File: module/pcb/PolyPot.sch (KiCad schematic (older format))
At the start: 43 parts, among them J1 V_BAT_1S, J2 PROG/DEBUG, J3 HUMIDITY_CONN, J4 TOF_DIST_SENS, J5 M3, J6 M3, J7 M3, J8 M3, J9 LUMINOSITY_CONN, M1 DC_WATER_PUMP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

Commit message: PCB: change SOIC-8 footprint
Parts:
- U4: footprint Housings_SOIC:SO-8_5.3x6.2mm_Pitch1.27mm -> Housings_SOIC:SOIC-8_3.9x4.9mm_Pitch1.27mm
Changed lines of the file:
@@
 F 0 "U4" H 4950 1650 60  0000 C CNN
 F 1 "BD6211F-E2" H 5650 1650 60  0000 C CNN
-F 2 "Housings_SOIC:SO-8_5.3x6.2mm_Pitch1.27mm" H 5300 1400 60  0001 C CNN
+F 2 "Housings_SOIC:SOIC-8_3.9x4.9mm_Pitch1.27mm" H 5300 1400 60  0001 C CNN
 F 3 "" H 5300 1400 60  0001 C CNN
 	1    5300 1400

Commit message: Add logo
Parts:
- removed TP1, TP2, TP3, TP4, TP5: TEST, Socket_Strips:Socket_Strip_Straight_1x01_Pitch1.27mm, symbol TEST
- added J10: I2C_TEST, Pin_Headers:Pin_Header_Straight_1x02_Pitch2.54mm, symbol Conn_01x02
- BT1, M1: footprint Socket_Strips:Socket_Strip_Straight_1x02_Pitch2.54mm -> Pin_Headers:Pin_Header_Straight_1x02_Pitch2.54mm
- J1: footprint Socket_Strips:Socket_Strip_Straight_1x01_Pitch2.54mm -> Pin_Headers:Pin_Header_Straight_1x01
- J2: footprint Socket_Strips:Socket_Strip_Straight_1x06_Pitch2.00mm -> Pin_Headers:Pin_Header_Straight_1x06_Pitch2.00mm
- J3, J9: footprint Socket_Strips:Socket_Strip_Straight_1x03_Pitch2.00mm -> Pin_Headers:Pin_Header_Straight_1x03_Pitch2.54mm
- J4: footprint Socket_Strips:Socket_Strip_Straight_1x05_Pitch2.00mm -> Pin_Headers:Pin_Header_Straight_1x05_Pitch2.54mm
- JP1, JP2: footprint Socket_Strips:Socket_Strip_Straight_1x02_Pitch1.27mm -> Pin_Headers:Pin_Header_Straight_1x02_Pitch2.54mm
- Q2: footprint TO_SOT_Packages_SMD:SOT-23 -> TO_SOT_Packages_SMD:SOT-23_Handsoldering
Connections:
- net I2C_SCL: now also J10.1 (Pin_1)
- net I2C_SDA: now also J10.2 (Pin_2)
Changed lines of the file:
@@
 LIBS:valves
 LIBS:PolyPot
+LIBS:PolyPot-cache
 EELAYER 25 0
 EELAYER END
@@
 F 0 "BT1" H 1200 1450 50  0000 L CNN
 F 1 "Battery" H 1200 1350 50  0000 L CNN
-F 2 "Socket_Strips:Socket_Strip_Straight_1x02_Pitch2.54mm" V 1100 1410 50  0001 C CNN
+F 2 "Pin_Headers:Pin_Header_Straight_1x02_Pitch2.54mm" V 1100 1410 50  0001 C CNN
 F 3 "" V 1100 1410 50  0001 C CNN
 	1    1100 1350
@@
 F 0 "JP1" H 1550 1230 50  0000 C CNN
 F 1 "I_SENSE" H 1560 1090 50  0000 C CNN
-F 2 "Socket_Strips:Socket_Strip_Straight_1x02_Pitch1.27mm" H 1550 1150 50  0001 C CNN
+F 2 "Pin_Headers:Pin_Header_Straight_1x02_Pitch2.54mm" H 1550 1150 50  0001 C CNN
 F 3 "" H 1550 1150 50  0001 C CNN
 	1    1550 1150
@@
 	1    0    0    -1
 $EndComp
-Text Label 8250 3350 2    60   ~ 0
+Text Label 7050 3300 0    60   ~ 0
 I2C_SDA
-Text Label 8250 3200 2    60   ~ 0
+Text Label 7050 3200 0    60   ~ 0
 I2C_SCL
 $Comp
@@
 F 0 "Q2" H 7950 1450 50  0000 L CNN
 F 1 "PMV250EPEAR" H 7950 1350 50  0000 L CNN
-F 2 "TO_SOT_Packages_SMD:SOT-23" H 7950 1500 50  0001 C CNN
+F 2 "TO_SOT_Packages_SMD:SOT-23_Handsoldering" H 7950 1500 50  0001 C CNN
 F 3 "" H 7750 1400 50  0001 C CNN
 	1    7750 1400
@@
 $EndComp
 $Comp
-L TEST TP2
-U 1 1 59FFB685
-P 7250 3200
-F 0 "TP2" H 7250 3500 50  0000 C BNN
-F 1 "TEST" H 7250 3450 50  0000 C CNN
-F 2 "Socket_Strips:Socket_Strip_Straight_1x01_Pitch1.27mm" H 7250 3200 50  0001 C CNN
-F 3 "" H 7250 3200 50  0001 C CNN
-	1    7250 3200
-	1    0    0    -1
-$EndComp
-$Comp
-L TEST TP1
-U 1 1 59FFB782
-P 7050 3350
-F 0 "TP1" H 7050 3650 50  0000 C BNN
-F 1 "TEST" H 7050 3600 50  0000 C CNN
-F 2 "Socket_Strips:Socket_Strip_Straight_1x01_Pitch1.27mm" H 7050 3350 50  0001 C CNN
-F 3 "" H 7050 3350 50  0001 C CNN
-	1    7050 3350
-	1    0    0    -1
-$EndComp
-$Comp
 L Jumper_NC_Small JP2
 U 1 1 59FFBC93
@@
 F 0 "JP2" H 8200 1380 50  0000 C CNN
 F 1 "I_SENSE" H 8210 1240 50  0000 C CNN
-F 2 "Socket_Strips:Socket_Strip_Straight_1x02_Pitch1.27mm" H 8200 1300 50  0001 C CNN
+F 2 "Pin_Headers:Pin_Header_Straight_1x02_Pitch2.54mm" H 8200 1300 50  0001 C CNN
 F 3 "" H 8200 1300 50  0001 C CNN
 	1    8200 1300
@@
 F 0 "J4" H 10300 3350 50  0000 C CNN
 F 1 "TOF_DIST_SENS" H 10300 2750 50  0000 C CNN
-F 2 "Socket_Strips:Socket_Strip_Straight_1x05_Pitch2.00mm" H 10300 3050 50  0001 C CNN
+F 2 "Pin_Headers:Pin_Header_Straight_1x05_Pitch2.54mm" H 10300 3050 50  0001 C CNN
 F 3 "" H 10300 3050 50  0001 C CNN
 	1    10300 3050
@@
 F 0 "M1" H 6200 1600 50  0000 L CNN
 F 1 "DC_WATER_PUMP" H 6200 1300 50  0000 L TNN
-F 2 "Socket_Strips:Socket_Strip_Straight_1x02_Pitch2.54mm" H 6100 1410 50  0001 C CNN
+F 2 "Pin_Headers:Pin_Header_Straight_1x02_Pitch2.54mm" H 6100 1410 50  0001 C CNN
 F 3 "" H 6100 1410 50  0001 C CNN
 	1    6100 1500
@@
 F 0 "J3" H 10300 2350 50  0000 C CNN
 F 1 "HUMIDITY_CONN" H 10300 1950 50  0000 C CNN
-F 2 "Socket_Strips:Socket_Strip_Straight_1x03_Pitch2.00mm" H 10300 2150 50  0001 C CNN
+F 2 "Pin_Headers:Pin_Header_Straight_1x03_Pitch2.54mm" H 10300 2150 50  0001 C CNN
 F 3 "" H 10300 2150 50  0001 C CNN
 	1    10300 2150
-	1    0    0    -1
-$EndComp
-$Comp
-L TEST TP3
-U 1 1 5A0459F4
-P 7700 5050
-F 0 "TP3" H 7700 5350 50  0000 C BNN
-F 1 "TEST" H 7700 5300 50  0000 C CNN
-F 2 "Socket_Strips:Socket_Strip_Straight_1x01_Pitch1.27mm" H 7700 5050 50  0001 C CNN
-F 3 "" H 7700 5050 50  0001 C CNN
-	1    7700 5050
-	1    0    0    -1
-$EndComp
-$Comp
-L TEST TP4
-U 1 1 5A045AFD
-P 7700 5950
-F 0 "TP4" H 7700 6250 50  0000 C BNN
-F 1 "TEST" H 7700 6200 50  0000 C CNN
-F 2 "Socket_Strips:Socket_Strip_Straight_1x01_Pitch1.27mm" H 7700 5950 50  0001 C CNN
-F 3 "" H 7700 5950 50  0001 C CNN
-	1    7700 5950
 	1    0    0    -1
 $EndComp
@@
 F 0 "J2" H 10300 4550 50  0000 C CNN
 F 1 "PROG/DEBUG" H 10300 3850 50  0000 C CNN
-F 2 "Socket_Strips:Socket_Strip_Straight_1x06_Pitch2.00mm" H 10300 4250 50  0001 C CNN
+F 2 "Pin_Headers:Pin_Header_Straight_1x06_Pitch2.00mm" H 10300 4250 50  0001 C CNN
 F 3 "" H 10300 4250 50  0001 C CNN
 	1    10300 4250
@@
 F 0 "J1" H 1450 2150 50  0000 C CNN
 F 1 "V_BAT_1S" H 1450 1950 50  0000 C CNN
-F 2 "Socket_Strips:Socket_Strip_Straight_1x01_Pitch2.54mm" H 1450 2050 50  0001 C CNN
+F 2 "Pin_Headers:Pin_Header_Straight_1x01" H 1450 2050 50  0001 C CNN
 F 3 "" H 1450 2050 50  0001 C CNN
 	1    1450 2050
@@
 	1    0    0    -1
 $EndComp
-$Comp
-L TEST TP5
-U 1 1 5A0B64C6
-P 7650 4250
-F 0 "TP5" H 7650 4550 50  0000 C BNN
-F 1 "TEST" H 7650 4500 50  0000 C CNN
-F 2 "Socket_Strips:Socket_Strip_Straight_1x01_Pitch1.27mm" H 7650 4250 50  0001 C CNN
-F 3 "" H 7650 4250 50  0001 C CNN
-	1    7650 4250
-	1    0    0    -1
-$EndComp
 Text Label 9300 1200 0    60   ~ 0
 3V3_SENSORS
@@
 F 0 "J9" H 10300 1500 50  0000 C CNN
 F 1 "LUMINOSITY_CONN" H 10300 1100 50  0000 C CNN
-F 2 "Socket_Strips:Socket_Strip_Straight_1x03_Pitch2.00mm" H 10300 1300 50  0001 C CNN
+F 2 "Pin_Headers:Pin_Header_Straight_1x03_Pitch2.54mm" H 10300 1300 50  0001 C CNN
 F 3 "" H 10300 1300 50  0001 C CNN
 	1    10300 1300
@@
 	7450 5850 7450 5950
 Wire Wire Line
-	7250 5950 8150 5950
-Wire Wire Line
 	9650 4150 10100 4150
 Wire Wire Line
@@
 Connection ~ 7700 2850
 Wire Wire Line
-	7600 3150 7600 3350
-Wire Wire Line
-	7050 3350 8250 3350
+	7600 3150 7600 3300
+Wire Wire Line
+	7050 3300 8100 3300
 Wire Wire Line
 	7800 3150 7800 3200
 Wire Wire Line
-	7250 3200 8250 3200
+	7050 3200 8100 3200
 Wire Wire Line
 	7400 1200 7400 1300
@@
 	7750 1800 7100 1800
 Connection ~ 7800 3200
-Connection ~ 7600 3350
+Connection ~ 7600 3300
 Wire Wire Line
 	9050 1300 8300 1300
@@
 	6700 5050 6800 5050
 Connection ~ 7450 5050
-Connection ~ 7700 5950
-Connection ~ 7700 5050
 Wire Wire Line
 	9100 5150 10450 5150
@@
 Wire Wire Line
 	6700 4250 6800 4250
-Wire Wire Line
-	7200 4250 8350 4250
 Connection ~ 7400 4250
-Connection ~ 7650 4250
 Wire Wire Line
 	9300 1200 10100 1200
@@
 Wire Wire Line
 	2900 3700 3000 3700
+Wire Wire Line
+	7200 4250 8350 4250
+Wire Wire Line
+	7250 5950 8150 5950
+$Comp
+L Conn_01x02 J10
+U 1 1 5A17AFB6
+P 8300 3200
+F 0 "J10" H 8300 3300 50  0000 C CNN
+F 1 "I2C_TEST" H 8300 3000 50  0000 C CNN
+F 2 "Pin_Headers:Pin_Header_Straight_1x02_Pitch2.54mm" H 8300 3200 50  0001 C CNN
+F 3 "" H 8300 3200 50  0001 C CNN
+	1    8300 3200
+	1    0    0    -1
+$EndComp
 $EndSCHEMATC

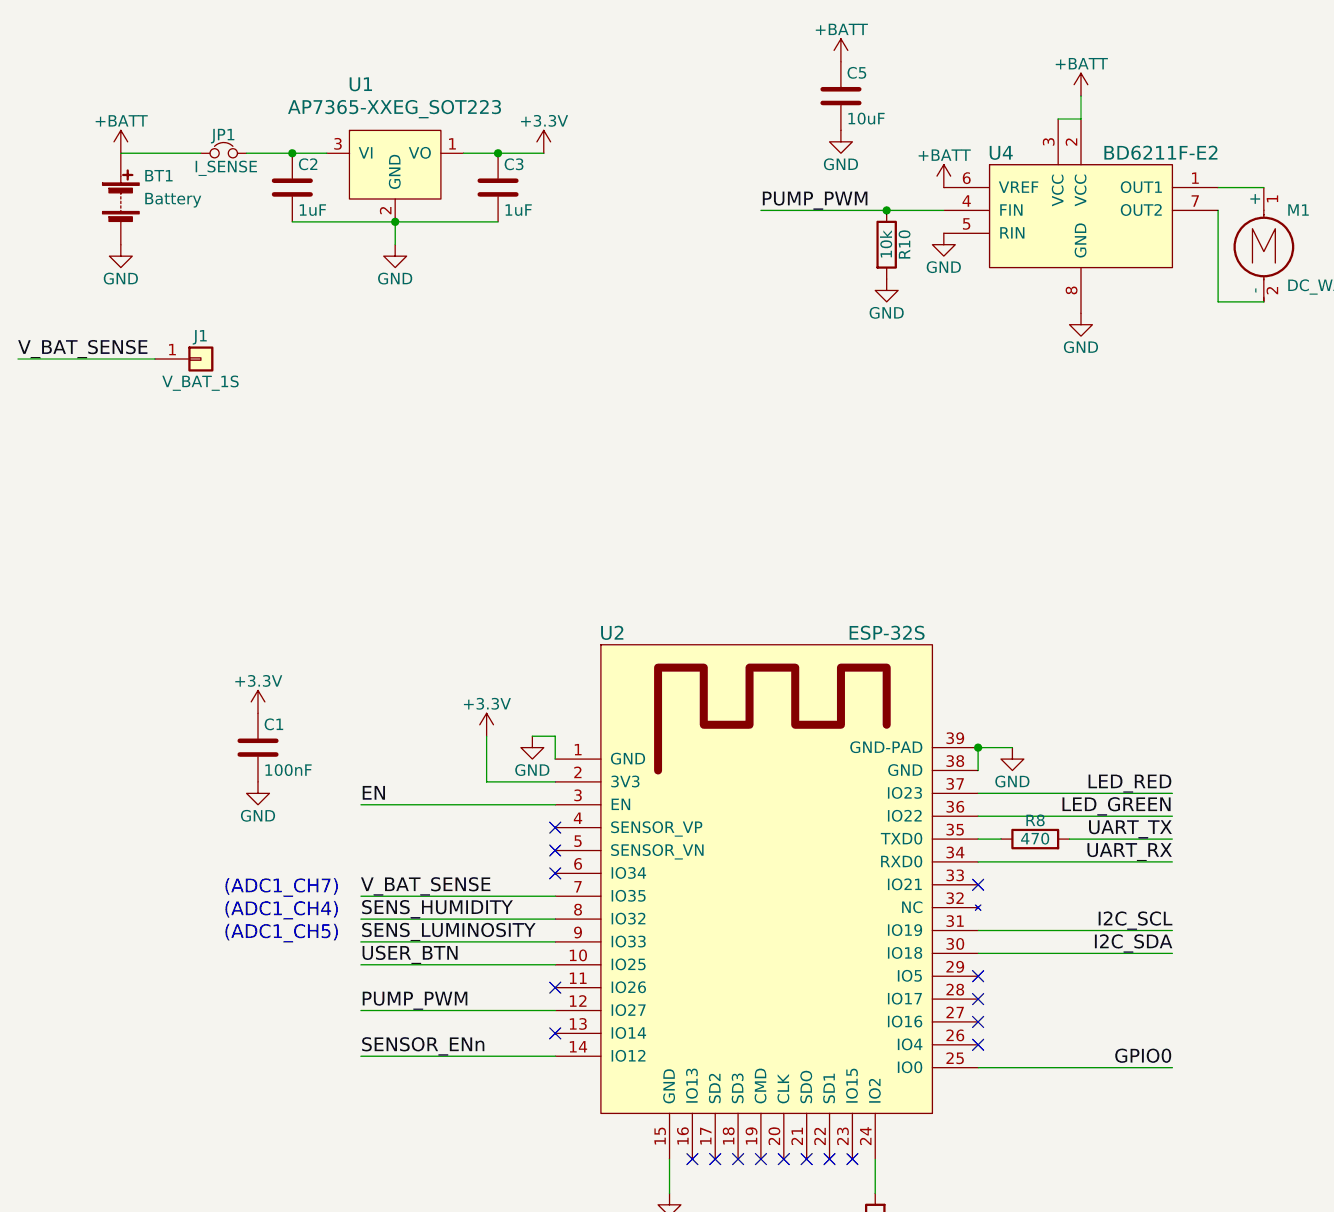
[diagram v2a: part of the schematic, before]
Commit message: PCB: fix 3.3V regulator footprint, connect TOF GPIO0, start routing
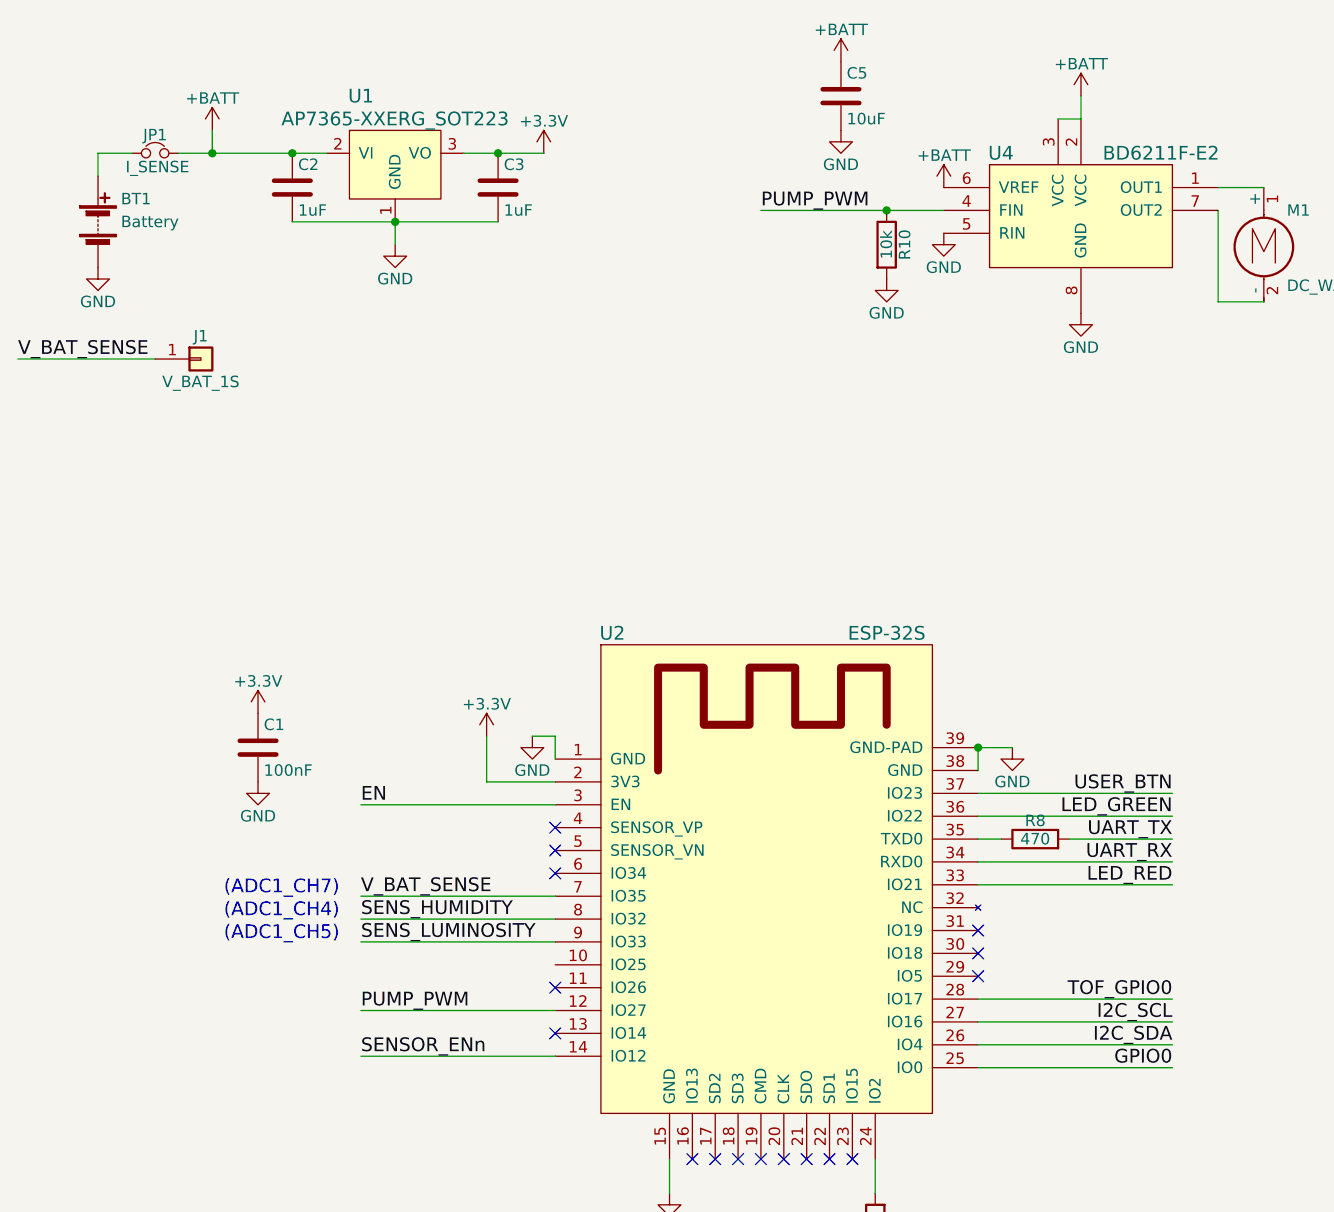
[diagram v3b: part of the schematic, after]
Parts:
- removed U1: AP7365-XXEG_SOT223, TO_SOT_Packages_SMD:SOT-223, symbol AP7365-XXEG_SOT223
- added U1: AP7365-XXERG_SOT223, TO_SOT_Packages_SMD:SOT-223, symbol AP7365-XXERG_SOT223
- J1: footprint Pin_Headers:Pin_Header_Straight_1x01 -> Pin_Headers:Pin_Header_Straight_1x01_Pitch2.54mm
- J2: footprint Pin_Headers:Pin_Header_Straight_1x06_Pitch2.00mm -> Pin_Headers:Pin_Header_Straight_1x06_Pitch2.54mm
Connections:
- net +3V3: now also U1.3 (VO)
- net +BATT: now also C2.1, JP1.2, U1.2 (VI); no longer BT1.1 (+), JP1.1
- net GND: now also U1.1 (GND)
- net I2C_SCL: now also U2.27 (IO16); no longer U2.31 (IO19)
- net I2C_SDA: now also U2.26 (IO4); no longer U2.30 (IO18)
- net LED_RED: now also U2.33 (IO21); no longer U2.37 (IO23)
- net TOF_GPIO0: now also U2.28 (IO17)
- net USER_BTN: now also U2.37 (IO23); no longer U2.10 (IO25)
- new net: BT1.1 (+), JP1.1
- no-connect marks 22 -> 20
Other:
- moved on the sheet: BT1, JP1
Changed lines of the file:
@@
 L Battery BT1
 U 1 1 59FEEA16
-P 1100 1350
-F 0 "BT1" H 1200 1450 50  0000 L CNN
-F 1 "Battery" H 1200 1350 50  0000 L CNN
-F 2 "Pin_Headers:Pin_Header_Straight_1x02_Pitch2.54mm" V 1100 1410 50  0001 C CNN
-F 3 "" V 1100 1410 50  0001 C CNN
-	1    1100 1350
+P 1000 1450
+F 0 "BT1" H 1100 1550 50  0000 L CNN
+F 1 "Battery" H 1100 1450 50  0000 L CNN
+F 2 "Pin_Headers:Pin_Header_Straight_1x02_Pitch2.54mm" V 1000 1510 50  0001 C CNN
+F 3 "" V 1000 1510 50  0001 C CNN
+	1    1000 1450
 	1    0    0    -1
 $EndComp
@@
 L GND #PWR03
 U 1 1 59FF3B77
-P 1100 1550
-F 0 "#PWR03" H 1100 1300 50  0001 C CNN
-F 1 "GND" H 1100 1400 50  0000 C CNN
-F 2 "" H 1100 1550 50  0001 C CNN
-F 3 "" H 1100 1550 50  0001 C CNN
-	1    1100 1550
+P 1000 1650
+F 0 "#PWR03" H 1000 1400 50  0001 C CNN
+F 1 "GND" H 1000 1500 50  0000 C CNN
+F 2 "" H 1000 1650 50  0001 C CNN
+F 3 "" H 1000 1650 50  0001 C CNN
+	1    1000 1650
 	1    0    0    -1
 $EndComp
@@
 L Jumper_NC_Small JP1
 U 1 1 59FF5D46
-P 1550 1150
-F 0 "JP1" H 1550 1230 50  0000 C CNN
-F 1 "I_SENSE" H 1560 1090 50  0000 C CNN
-F 2 "Pin_Headers:Pin_Header_Straight_1x02_Pitch2.54mm" H 1550 1150 50  0001 C CNN
-F 3 "" H 1550 1150 50  0001 C CNN
-	1    1550 1150
+P 1250 1150
+F 0 "JP1" H 1250 1230 50  0000 C CNN
+F 1 "I_SENSE" H 1260 1090 50  0000 C CNN
+F 2 "Pin_Headers:Pin_Header_Straight_1x02_Pitch2.54mm" H 1250 1150 50  0001 C CNN
+F 3 "" H 1250 1150 50  0001 C CNN
+	1    1250 1150
 	1    0    0    -1
 $EndComp
@@
 F 0 "J2" H 10300 4550 50  0000 C CNN
 F 1 "PROG/DEBUG" H 10300 3850 50  0000 C CNN
-F 2 "Pin_Headers:Pin_Header_Straight_1x06_Pitch2.00mm" H 10300 4250 50  0001 C CNN
+F 2 "Pin_Headers:Pin_Header_Straight_1x06_Pitch2.54mm" H 10300 4250 50  0001 C CNN
 F 3 "" H 10300 4250 50  0001 C CNN
 	1    10300 4250
@@
 F 0 "J1" H 1450 2150 50  0000 C CNN
 F 1 "V_BAT_1S" H 1450 1950 50  0000 C CNN
-F 2 "Pin_Headers:Pin_Header_Straight_1x01" H 1450 2050 50  0001 C CNN
+F 2 "Pin_Headers:Pin_Header_Straight_1x01_Pitch2.54mm" H 1450 2050 50  0001 C CNN
 F 3 "" H 1450 2050 50  0001 C CNN
 	1    1450 2050
@@
 $EndComp
 $Comp
-L AP7365-XXEG_SOT223 U1
-U 1 1 5A0DAEAA
-P 2300 1150
-F 0 "U1" H 2150 1450 60  0000 C CNN
-F 1 "AP7365-XXEG_SOT223" H 2300 1350 60  0000 C CNN
-F 2 "TO_SOT_Packages_SMD:SOT-223" H 2300 1150 60  0001 C CNN
-F 3 "" H 2300 1150 60  0001 C CNN
-	1    2300 1150
-	1    0    0    -1
-$EndComp
-$Comp
 L ESP-32S U2
 U 1 1 5A131A94
@@
 Text Label 5700 4250 2    60   ~ 0
 UART_RX
-Text Label 5700 4550 2    60   ~ 0
+Text Label 5700 4950 2    60   ~ 0
 I2C_SCL
-Text Label 5700 4650 2    60   ~ 0
+Text Label 5700 5050 2    60   ~ 0
 I2C_SDA
 Text Label 5700 5150 2    60   ~ 0
@@
 Text Label 2150 4600 0    60   ~ 0
 SENS_LUMINOSITY
-Text Label 2150 4700 0    60   ~ 0
+Text Label 5700 3950 2    60   ~ 0
 USER_BTN
 Text Label 2150 5100 0    60   ~ 0
@@
 L +BATT #PWR029
 U 1 1 5A16E00E
-P 1100 1150
-F 0 "#PWR029" H 1100 1000 50  0001 C CNN
-F 1 "+BATT" H 1100 1290 50  0000 C CNN
-F 2 "" H 1100 1150 50  0001 C CNN
-F 3 "" H 1100 1150 50  0001 C CNN
-	1    1100 1150
+P 1500 1050
+F 0 "#PWR029" H 1500 900 50  0001 C CNN
+F 1 "+BATT" H 1500 1190 50  0000 C CNN
+F 2 "" H 1500 1050 50  0001 C CNN
+F 3 "" H 1500 1050 50  0001 C CNN
+	1    1500 1050
 	1    0    0    -1
 $EndComp
@@
 $EndComp
 Wire Wire Line
-	1100 1150 1450 1150
-Wire Wire Line
-	1650 1150 2000 1150
+	1000 1150 1150 1150
+Wire Wire Line
+	1350 1150 2000 1150
 Connection ~ 1850 1150
 Connection ~ 2750 1150
@@
 	2150 4600 3000 4600
 Wire Wire Line
-	2150 4700 3000 4700
+	4850 4350 5700 4350
 Wire Wire Line
 	2150 4900 3000 4900
@@
 	4850 5150 5700 5150
 Wire Wire Line
-	4850 4650 5700 4650
-Wire Wire Line
-	4850 4550 5700 4550
+	4850 5050 5700 5050
+Wire Wire Line
+	4850 4950 5700 4950
 Wire Wire Line
 	4850 4250 5700 4250
@@
 Wire Wire Line
 	2800 6600 3400 6600
-Text Label 5700 3950 2    60   ~ 0
+Text Label 5700 4350 2    60   ~ 0
 LED_RED
 Text Label 5700 4050 2    60   ~ 0
@@
 Wire Wire Line
 	4850 3950 5700 3950
-NoConn ~ 4850 4350
 NoConn ~ 4850 4750
-NoConn ~ 4850 4850
-NoConn ~ 4850 4950
-NoConn ~ 4850 5050
+NoConn ~ 4850 4550
+NoConn ~ 4850 4650
 NoConn ~ 4300 5550
 NoConn ~ 4200 5550
@@
 	1    0    0    -1
 $EndComp
+Wire Wire Line
+	1500 1050 1500 1150
+Connection ~ 1500 1150
+Wire Wire Line
+	1000 1150 1000 1250
+$Comp
+L AP7365-XXERG_SOT223 U1
+U 1 1 5A1794F0
+P 2300 1150
+F 0 "U1" H 2150 1400 60  0000 C CNN
+F 1 "AP7365-XXERG_SOT223" H 2300 1300 60  0000 C CNN
+F 2 "TO_SOT_Packages_SMD:SOT-223" H 2300 1150 60  0001 C CNN
+F 3 "" H 2300 1150 60  0001 C CNN
+	1    2300 1150
+	1    0    0    -1
+$EndComp
+Text Label 5700 4850 2    60   ~ 0
+TOF_GPIO0
+Wire Wire Line
+	5700 4850 4850 4850
 $EndSCHEMATC

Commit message: PCB: routing almost done, silkscreen text
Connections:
- net SENS_LUMINOSITY: now also U2.7 (IO35); no longer U2.9 (IO33)
- net V_BAT_SENSE: now also U2.9 (IO33); no longer U2.7 (IO35)
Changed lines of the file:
@@
 Text Label 2150 4000 0    60   ~ 0
 EN
-Text Label 2150 4400 0    60   ~ 0
+Text Label 2150 4600 0    60   ~ 0
 V_BAT_SENSE
 Text Label 2150 4500 0    60   ~ 0
 SENS_HUMIDITY
-Text Label 2150 4600 0    60   ~ 0
+Text Label 2150 4400 0    60   ~ 0
 SENS_LUMINOSITY
 Text Label 5700 3950 2    60   ~ 0
